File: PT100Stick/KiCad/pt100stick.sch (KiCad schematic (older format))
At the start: 10 parts, among them U1 MAX31865ATP_

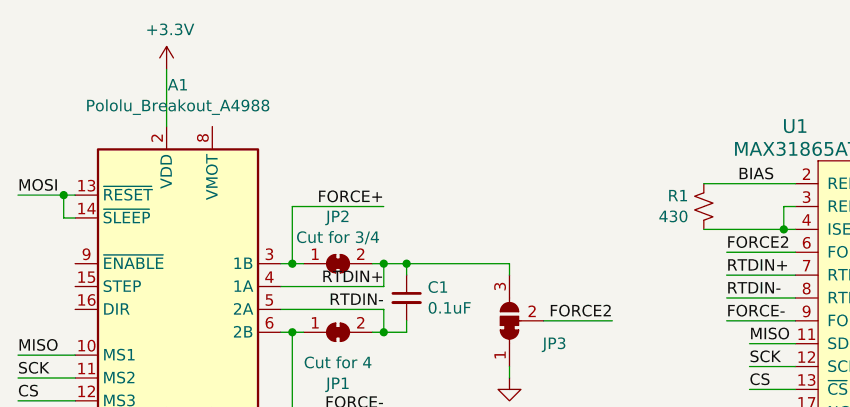
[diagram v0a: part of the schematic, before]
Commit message: move edgecuts
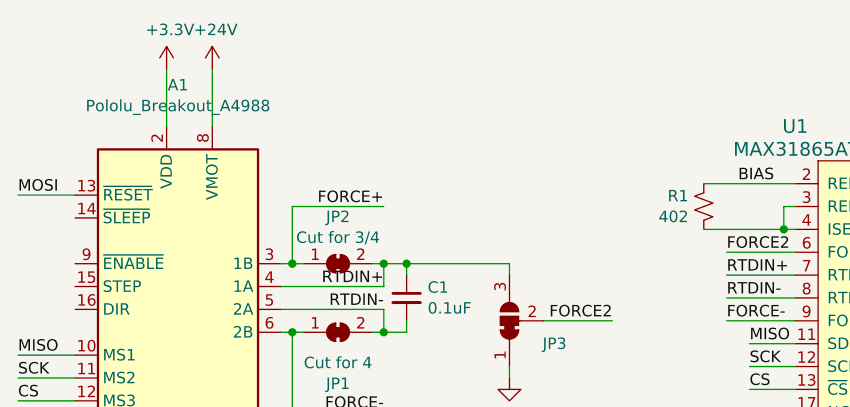
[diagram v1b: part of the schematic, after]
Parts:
- R1: value 430 -> 402
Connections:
- net MOSI: no longer A1.14 (~SLEEP)
- net +24V: now reaches A1.8 (VMOT)
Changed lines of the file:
@@
 EESchema Schematic File Version 4
+LIBS:pt100stick-cache
 EELAYER 30 0
 EELAYER END
@@
 Text Label 1250 2550 0    50   ~ 0
 CS
-Wire Wire Line
-	1500 1750 1450 1750
-Wire Wire Line
-	1450 1750 1450 1650
-Wire Wire Line
-	1450 1650 1500 1650
-Wire Wire Line
-	1250 1650 1450 1650
-Connection ~ 1450 1650
 Text Label 1250 2450 0    50   ~ 0
 SCK
@@
 P 4250 1700
 F 0 "R1" H 4183 1654 50  0000 R CNN
-F 1 "430" H 4183 1745 50  0000 R CNN
+F 1 "402" H 4183 1745 50  0000 R CNN
 F 2 "PT100Stick:R_0603_1608Metric_Pad1.05x0.95mm_HandSolder" H 4250 1700 50  0001 C CNN
 F 3 "~" H 4250 1700 50  0001 C CNN
@@
 	1    0    0    -1
 $EndComp
+Wire Wire Line
+	1250 1650 1500 1650
+$Comp
+L power:+24V #PWR0113
+U 1 1 5F580864
+P 2100 1100
+F 0 "#PWR0113" H 2100 950 50  0001 C CNN
+F 1 "+24V" H 2115 1273 50  0000 C CNN
+F 2 "" H 2100 1100 50  0001 C CNN
+F 3 "" H 2100 1100 50  0001 C CNN
+	1    2100 1100
+	1    0    0    -1
+$EndComp
+Wire Wire Line
+	2100 1100 2100 1350
 $EndSCHEMATC

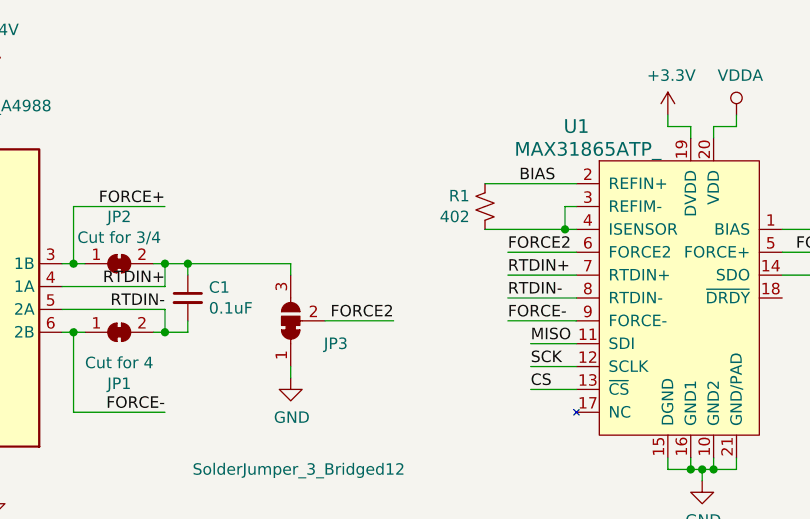
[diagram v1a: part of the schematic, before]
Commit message: Add tolerance to sense resistor
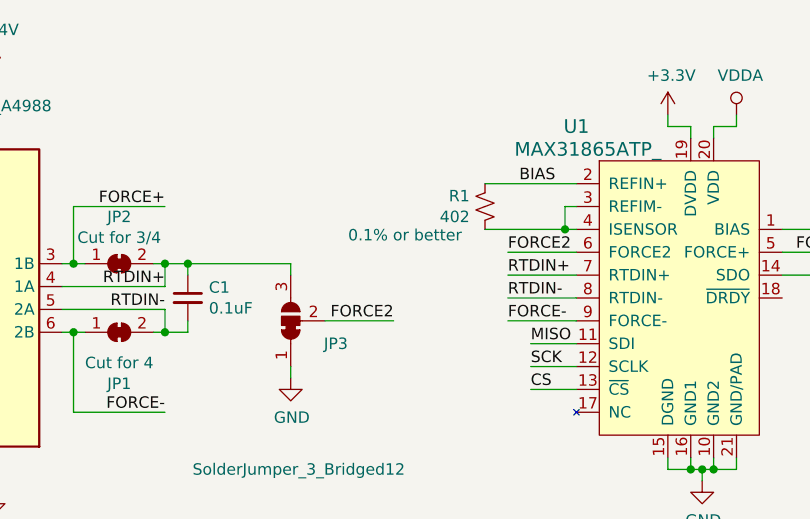
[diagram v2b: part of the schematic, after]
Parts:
- R1: Tolerance (none) -> 0.1% or better
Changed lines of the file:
@@
 F 2 "PT100Stick:R_0603_1608Metric_Pad1.05x0.95mm_HandSolder" H 4250 1700 50  0001 C CNN
 F 3 "~" H 4250 1700 50  0001 C CNN
+F 4 "0.1% or better" H 3900 1825 50  0000 C CNN "Tolerance"
 	1    4250 1700
 	1    0    0    1

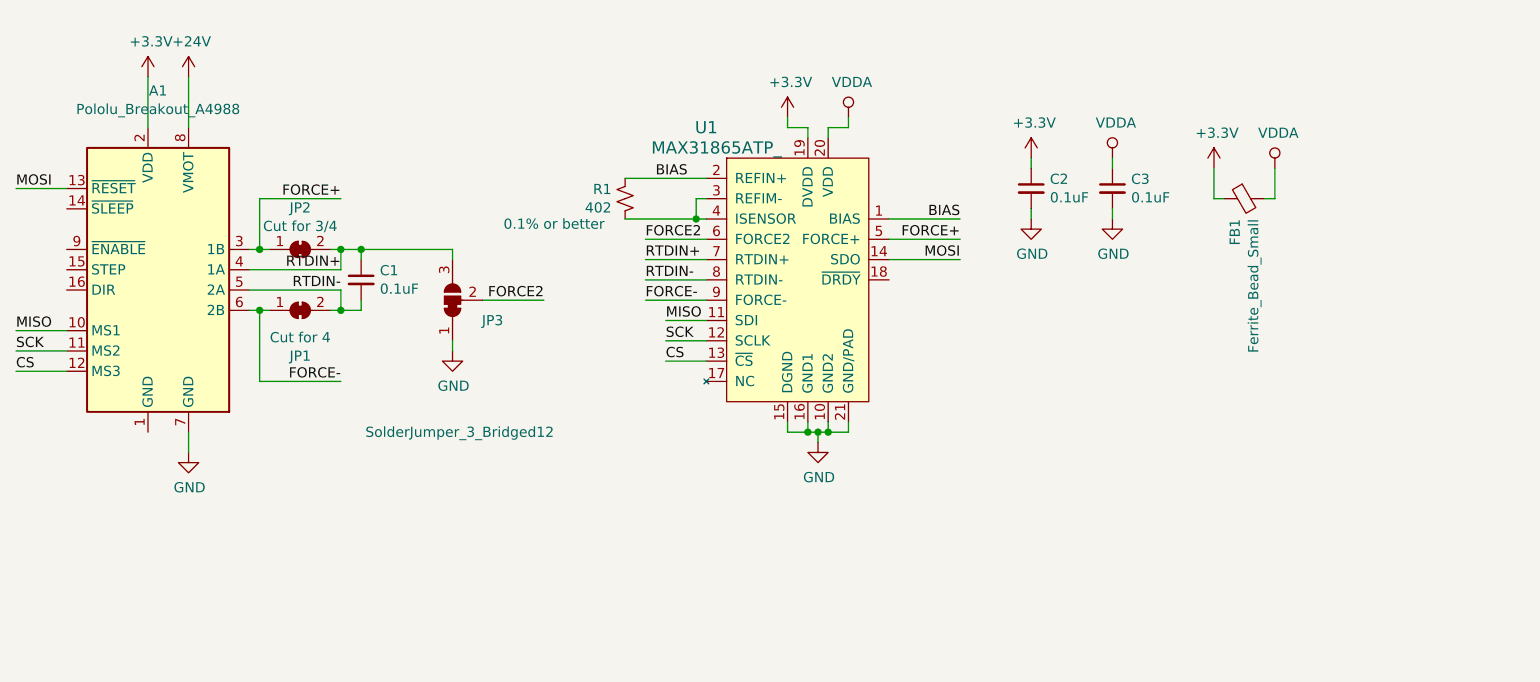
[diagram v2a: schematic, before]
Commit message: Add 3v3 reg for better board compatibility.
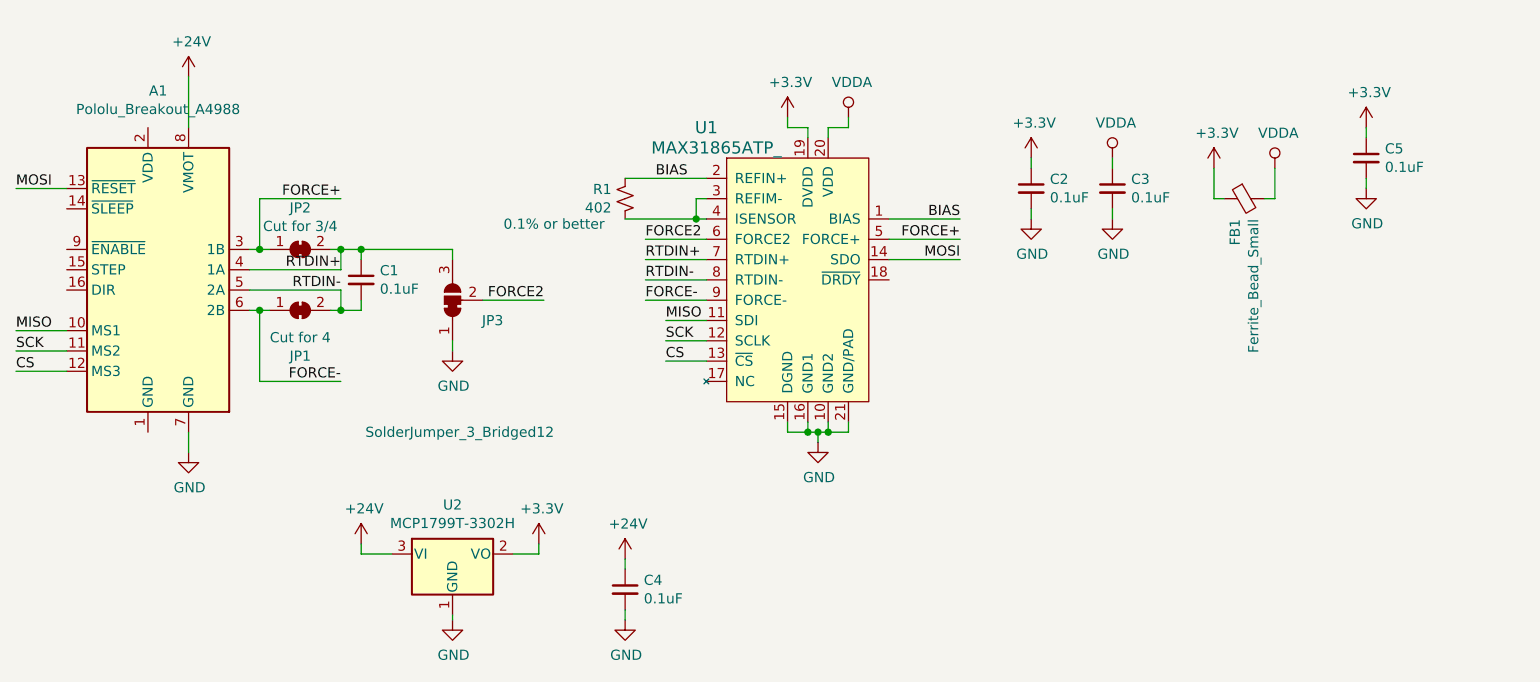
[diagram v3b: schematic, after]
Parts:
- added C4, C5: 0.1uF, PT100Stick:C_0603_1608Metric_Pad1.05x0.95mm_HandSolder, symbol PT100stick:C_Small
- added U2: MCP1799T-3302H, Package_TO_SOT_SMD:SOT-23, symbol Regulator_Linear:MCP1700-3302E_SOT23
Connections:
- net +24V: now also C4.1, U2.3 (VI)
- net +3V3: now also C5.1, U2.2 (VO); no longer A1.2 (VDD)
- net GND: now also C4.2, C5.2, U2.1 (GND)
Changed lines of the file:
@@
 $EndComp
-$Comp
-L PT100stick:+3.3V #PWR0102
-U 1 1 5EBA1652
-P 1900 1100
-F 0 "#PWR0102" H 1900 950 50  0001 C CNN
-F 1 "+3.3V" H 1915 1273 50  0000 C CNN
-F 2 "" H 1900 1100 50  0001 C CNN
-F 3 "" H 1900 1100 50  0001 C CNN
-	1    1900 1100
-	1    0    0    -1
-$EndComp
-Wire Wire Line
-	1900 1100 1900 1350
 $Comp
 L PT100stick:MAX31865ATP_ U1
@@
 Wire Wire Line
 	2100 1100 2100 1350
+$Comp
+L Regulator_Linear:MCP1700-3302E_SOT23 U2
+U 1 1 5F6506B3
+P 3400 3450
+F 0 "U2" H 3400 3692 50  0000 C CNN
+F 1 "MCP1799T-3302H" H 3400 3601 50  0000 C CNN
+F 2 "Package_TO_SOT_SMD:SOT-23" H 3400 3675 50  0001 C CNN
+F 3 "http://ww1.microchip.com/downloads/en/DeviceDoc/20001826D.pdf" H 3400 3450 50  0001 C CNN
+	1    3400 3450
+	1    0    0    -1
+$EndComp
+$Comp
+L PT100stick:GND #PWR0114
+U 1 1 5F6513D1
+P 3400 3775
+F 0 "#PWR0114" H 3400 3525 50  0001 C CNN
+F 1 "GND" H 3405 3602 50  0000 C CNN
+F 2 "" H 3400 3775 50  0001 C CNN
+F 3 "" H 3400 3775 50  0001 C CNN
+	1    3400 3775
+	1    0    0    -1
+$EndComp
+$Comp
+L power:+24V #PWR0115
+U 1 1 5F652BAA
+P 2950 3400
+F 0 "#PWR0115" H 2950 3250 50  0001 C CNN
+F 1 "+24V" H 2965 3573 50  0000 C CNN
+F 2 "" H 2950 3400 50  0001 C CNN
+F 3 "" H 2950 3400 50  0001 C CNN
+	1    2950 3400
+	1    0    0    -1
+$EndComp
+Wire Wire Line
+	2950 3400 2950 3450
+Wire Wire Line
+	2950 3450 3100 3450
+$Comp
+L PT100stick:+3.3V #PWR0116
+U 1 1 5F655A3A
+P 3825 3400
+F 0 "#PWR0116" H 3825 3250 50  0001 C CNN
+F 1 "+3.3V" H 3840 3573 50  0000 C CNN
+F 2 "" H 3825 3400 50  0001 C CNN
+F 3 "" H 3825 3400 50  0001 C CNN
+	1    3825 3400
+	1    0    0    -1
+$EndComp
+Wire Wire Line
+	3700 3450 3825 3450
+Wire Wire Line
+	3825 3450 3825 3400
+$Comp
+L PT100stick:C_Small C4
+U 1 1 5F65B31E
+P 4250 3625
+F 0 "C4" H 4342 3671 50  0000 L CNN
+F 1 "0.1uF" H 4342 3580 50  0000 L CNN
+F 2 "PT100Stick:C_0603_1608Metric_Pad1.05x0.95mm_HandSolder" H 4250 3625 50  0001 C CNN
+F 3 "~" H 4250 3625 50  0001 C CNN
+	1    4250 3625
+	1    0    0    -1
+$EndComp
+Wire Wire Line
+	4250 3475 4250 3525
+Wire Wire Line
+	4250 3725 4250 3775
+$Comp
+L PT100stick:GND #PWR0117
+U 1 1 5F65B32C
+P 4250 3775
+F 0 "#PWR0117" H 4250 3525 50  0001 C CNN
+F 1 "GND" H 4255 3602 50  0000 C CNN
+F 2 "" H 4250 3775 50  0001 C CNN
+F 3 "" H 4250 3775 50  0001 C CNN
+	1    4250 3775
+	1    0    0    -1
+$EndComp
+$Comp
+L power:+24V #PWR0118
+U 1 1 5F65CFFD
+P 4250 3475
+F 0 "#PWR0118" H 4250 3325 50  0001 C CNN
+F 1 "+24V" H 4265 3648 50  0000 C CNN
+F 2 "" H 4250 3475 50  0001 C CNN
+F 3 "" H 4250 3475 50  0001 C CNN
+	1    4250 3475
+	1    0    0    -1
+$EndComp
+Wire Wire Line
+	3400 3750 3400 3775
+$Comp
+L PT100stick:C_Small C5
+U 1 1 5F665B61
+P 7900 1500
+F 0 "C5" H 7992 1546 50  0000 L CNN
+F 1 "0.1uF" H 7992 1455 50  0000 L CNN
+F 2 "PT100Stick:C_0603_1608Metric_Pad1.05x0.95mm_HandSolder" H 7900 1500 50  0001 C CNN
+F 3 "~" H 7900 1500 50  0001 C CNN
+	1    7900 1500
+	1    0    0    -1
+$EndComp
+Wire Wire Line
+	7900 1350 7900 1400
+Wire Wire Line
+	7900 1600 7900 1650
+$Comp
+L PT100stick:+3.3V #PWR0119
+U 1 1 5F665B69
+P 7900 1350
+F 0 "#PWR0119" H 7900 1200 50  0001 C CNN
+F 1 "+3.3V" H 7915 1523 50  0000 C CNN
+F 2 "" H 7900 1350 50  0001 C CNN
+F 3 "" H 7900 1350 50  0001 C CNN
+	1    7900 1350
+	1    0    0    -1
+$EndComp
+$Comp
+L PT100stick:GND #PWR0120
+U 1 1 5F665B6F
+P 7900 1650
+F 0 "#PWR0120" H 7900 1400 50  0001 C CNN
+F 1 "GND" H 7905 1477 50  0000 C CNN
+F 2 "" H 7900 1650 50  0001 C CNN
+F 3 "" H 7900 1650 50  0001 C CNN
+	1    7900 1650
+	1    0    0    -1
+$EndComp
 $EndSCHEMATC

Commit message: Add 2.2uF cap
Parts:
- removed FB1: Ferrite_Bead_Small, PT100Stick:L_0603_1608Metric_Pad1.05x0.95mm_HandSolder, symbol PT100stick:Ferrite_Bead_Small
- added C6: 2.2uF, PT100Stick:C_0603_1608Metric_Pad1.05x0.95mm_HandSolder, symbol PT100stick:C_Small
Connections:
- net VDDA is gone; now on net +3V3: C3.1, U1.20 (VDD)
- net +3V3: now also C6.1
- net GND: now also C6.2
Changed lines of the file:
@@
 	6250 1750 6250 1800
-$Comp
-L PT100stick:Ferrite_Bead_Small FB1
-U 1 1 5EC32E91
-P 7300 1700
-F 0 "FB1" H 7400 1746 50  0000 L CNN
-F 1 "Ferrite_Bead_Small" H 7400 1655 50  0000 L CNN
-F 2 "PT100Stick:L_0603_1608Metric_Pad1.05x0.95mm_HandSolder" V 7230 1700 50  0001 C CNN
-F 3 "~" H 7300 1700 50  0001 C CNN
-	1    7300 1700
-	0    -1   1    0
-$EndComp
-$Comp
-L PT100stick:+3.3V #PWR0103
-U 1 1 5EBCE55F
-P 7150 1550
-F 0 "#PWR0103" H 7150 1400 50  0001 C CNN
-F 1 "+3.3V" H 7165 1723 50  0000 C CNN
-F 2 "" H 7150 1550 50  0001 C CNN
-F 3 "" H 7150 1550 50  0001 C CNN
-	1    7150 1550
-	1    0    0    -1
-$EndComp
 $Comp
 L PT100stick:+3.3V #PWR0105
@@
 	1    0    0    -1
 $EndComp
-Wire Wire Line
-	7150 1700 7200 1700
-$Comp
-L power:VDDA #PWR0108
-U 1 1 5EBDF6C7
-P 7450 1550
-F 0 "#PWR0108" H 7450 1400 50  0001 C CNN
-F 1 "VDDA" H 7467 1723 50  0000 C CNN
-F 2 "" H 7450 1550 50  0001 C CNN
-F 3 "" H 7450 1550 50  0001 C CNN
-	1    7450 1550
-	1    0    0    -1
-$EndComp
-Wire Wire Line
-	7450 1550 7450 1700
-Wire Wire Line
-	7450 1700 7400 1700
-Wire Wire Line
-	7150 1550 7150 1700
 $Comp
 L PT100stick:+3.3V #PWR0109
@@
 	1    0    0    -1
 $EndComp
+$Comp
+L PT100stick:C_Small C6
+U 1 1 60650D3C
+P 8325 1500
+F 0 "C6" H 8417 1546 50  0000 L CNN
+F 1 "2.2uF" H 8417 1455 50  0000 L CNN
+F 2 "PT100Stick:C_0603_1608Metric_Pad1.05x0.95mm_HandSolder" H 8325 1500 50  0001 C CNN
+F 3 "~" H 8325 1500 50  0001 C CNN
+	1    8325 1500
+	1    0    0    -1
+$EndComp
+Wire Wire Line
+	8325 1350 8325 1400
+Wire Wire Line
+	8325 1600 8325 1650
+$Comp
+L PT100stick:+3.3V #PWR0102
+U 1 1 60650D44
+P 8325 1350
+F 0 "#PWR0102" H 8325 1200 50  0001 C CNN
+F 1 "+3.3V" H 8340 1523 50  0000 C CNN
+F 2 "" H 8325 1350 50  0001 C CNN
+F 3 "" H 8325 1350 50  0001 C CNN
+	1    8325 1350
+	1    0    0    -1
+$EndComp
+$Comp
+L PT100stick:GND #PWR0121
+U 1 1 60650D4A
+P 8325 1650
+F 0 "#PWR0121" H 8325 1400 50  0001 C CNN
+F 1 "GND" H 8330 1477 50  0000 C CNN
+F 2 "" H 8325 1650 50  0001 C CNN
+F 3 "" H 8325 1650 50  0001 C CNN
+	1    8325 1650
+	1    0    0    -1
+$EndComp
+$Comp
+L power:VDDA #PWR?
+U 1 1 60657271
+P 6725 1025
+F 0 "#PWR?" H 6725 875 50  0001 C CNN
+F 1 "VDDA" H 6742 1198 50  0000 C CNN
+F 2 "" H 6725 1025 50  0001 C CNN
+F 3 "" H 6725 1025 50  0001 C CNN
+	1    6725 1025
+	1    0    0    -1
+$EndComp
+$Comp
+L PT100stick:+3.3V #PWR?
+U 1 1 60658DCC
+P 6950 1025
+F 0 "#PWR?" H 6950 875 50  0001 C CNN
+F 1 "+3.3V" H 6965 1198 50  0000 C CNN
+F 2 "" H 6950 1025 50  0001 C CNN
+F 3 "" H 6950 1025 50  0001 C CNN
+	1    6950 1025
+	1    0    0    -1
+$EndComp
+Wire Wire Line
+	6725 1025 6725 1075
+Wire Wire Line
+	6725 1075 6950 1075
+Wire Wire Line
+	6950 1075 6950 1025
 $EndSCHEMATC
